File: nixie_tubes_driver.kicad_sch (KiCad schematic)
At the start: 17 parts, among them IC1 TPS61041DBVR, U1 CD40109BPW, U5 CD40109BPW, U6 HV5122PG-G, U7 HV5122PG-G

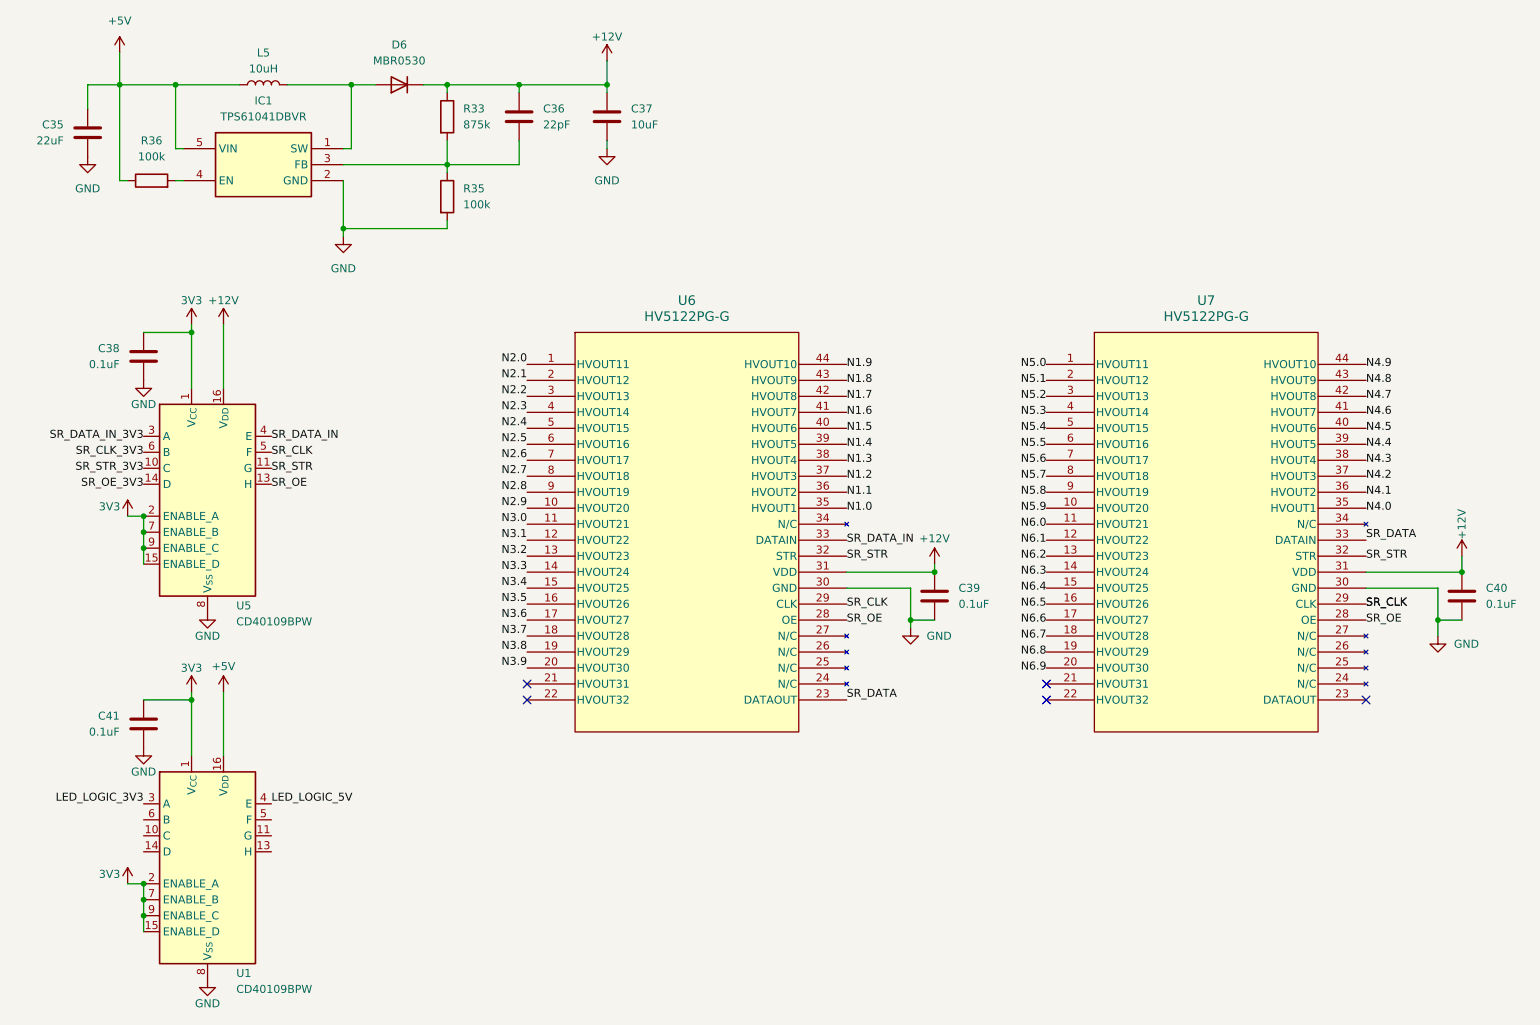
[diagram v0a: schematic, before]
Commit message: Add global labels for nets spanning several sheets
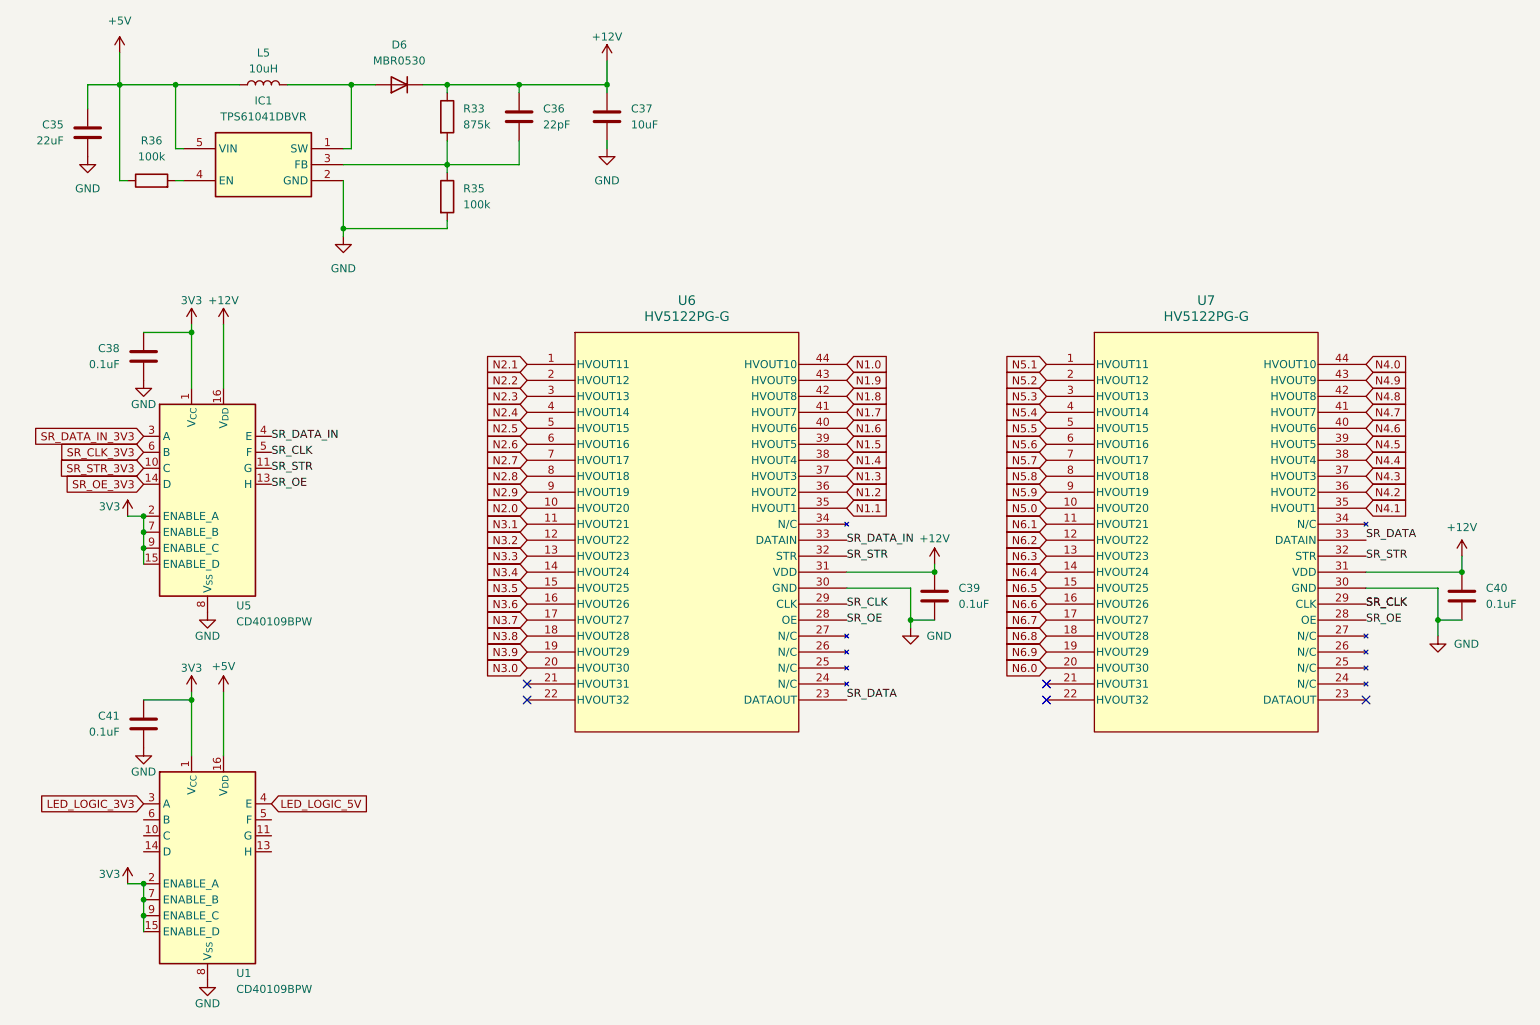
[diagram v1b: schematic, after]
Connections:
- net N1.0: now also U6.44 (HVOUT10); no longer U6.35 (HVOUT1)
- net N1.1: now also U6.35 (HVOUT1); no longer U6.36 (HVOUT2)
- net N1.2: now also U6.36 (HVOUT2); no longer U6.37 (HVOUT3)
- net N1.3: now also U6.37 (HVOUT3); no longer U6.38 (HVOUT4)
- net N1.4: now also U6.38 (HVOUT4); no longer U6.39 (HVOUT5)
- net N1.5: now also U6.39 (HVOUT5); no longer U6.40 (HVOUT6)
- net N1.6: now also U6.40 (HVOUT6); no longer U6.41 (HVOUT7)
- net N1.7: now also U6.41 (HVOUT7); no longer U6.42 (HVOUT8)
- net N1.8: now also U6.42 (HVOUT8); no longer U6.43 (HVOUT9)
- net N1.9: now also U6.43 (HVOUT9); no longer U6.44 (HVOUT10)
- net N2.0: now also U6.10 (HVOUT20); no longer U6.1 (HVOUT11)
- net N2.1: now also U6.1 (HVOUT11); no longer U6.2 (HVOUT12)
- net N2.2: now also U6.2 (HVOUT12); no longer U6.3 (HVOUT13)
- net N2.3: now also U6.3 (HVOUT13); no longer U6.4 (HVOUT14)
- net N2.4: now also U6.4 (HVOUT14); no longer U6.5 (HVOUT15)
- net N2.5: now also U6.5 (HVOUT15); no longer U6.6 (HVOUT16)
- net N2.6: now also U6.6 (HVOUT16); no longer U6.7 (HVOUT17)
- net N2.7: now also U6.7 (HVOUT17); no longer U6.8 (HVOUT18)
- net N2.8: now also U6.8 (HVOUT18); no longer U6.9 (HVOUT19)
- net N2.9: now also U6.9 (HVOUT19); no longer U6.10 (HVOUT20)
- net N3.0: now also U6.20 (HVOUT30); no longer U6.11 (HVOUT21)
- net N3.1: now also U6.11 (HVOUT21); no longer U6.12 (HVOUT22)
- net N3.2: now also U6.12 (HVOUT22); no longer U6.13 (HVOUT23)
- net N3.3: now also U6.13 (HVOUT23); no longer U6.14 (HVOUT24)
- net N3.4: now also U6.14 (HVOUT24); no longer U6.15 (HVOUT25)
- net N3.5: now also U6.15 (HVOUT25); no longer U6.16 (HVOUT26)
- net N3.6: now also U6.16 (HVOUT26); no longer U6.17 (HVOUT27)
- net N3.7: now also U6.17 (HVOUT27); no longer U6.18 (HVOUT28)
- net N3.8: now also U6.18 (HVOUT28); no longer U6.19 (HVOUT29)
- net N3.9: now also U6.19 (HVOUT29); no longer U6.20 (HVOUT30)
- net N4.0: now also U7.44 (HVOUT10); no longer U7.35 (HVOUT1)
- net N4.1: now also U7.35 (HVOUT1); no longer U7.36 (HVOUT2)
- net N4.2: now also U7.36 (HVOUT2); no longer U7.37 (HVOUT3)
- net N4.3: now also U7.37 (HVOUT3); no longer U7.38 (HVOUT4)
- net N4.4: now also U7.38 (HVOUT4); no longer U7.39 (HVOUT5)
- net N4.5: now also U7.39 (HVOUT5); no longer U7.40 (HVOUT6)
- net N4.6: now also U7.40 (HVOUT6); no longer U7.41 (HVOUT7)
- net N4.7: now also U7.41 (HVOUT7); no longer U7.42 (HVOUT8)
- net N4.8: now also U7.42 (HVOUT8); no longer U7.43 (HVOUT9)
- net N4.9: now also U7.43 (HVOUT9); no longer U7.44 (HVOUT10)
- net N5.0: now also U7.10 (HVOUT20); no longer U7.1 (HVOUT11)
- net N5.1: now also U7.1 (HVOUT11); no longer U7.2 (HVOUT12)
- net N5.2: now also U7.2 (HVOUT12); no longer U7.3 (HVOUT13)
- net N5.3: now also U7.3 (HVOUT13); no longer U7.4 (HVOUT14)
- net N5.4: now also U7.4 (HVOUT14); no longer U7.5 (HVOUT15)
- net N5.5: now also U7.5 (HVOUT15); no longer U7.6 (HVOUT16)
- net N5.6: now also U7.6 (HVOUT16); no longer U7.7 (HVOUT17)
- net N5.7: now also U7.7 (HVOUT17); no longer U7.8 (HVOUT18)
- net N5.8: now also U7.8 (HVOUT18); no longer U7.9 (HVOUT19)
- net N5.9: now also U7.9 (HVOUT19); no longer U7.10 (HVOUT20)
- net N6.0: now also U7.20 (HVOUT30); no longer U7.11 (HVOUT21)
- net N6.1: now also U7.11 (HVOUT21); no longer U7.12 (HVOUT22)
- net N6.2: now also U7.12 (HVOUT22); no longer U7.13 (HVOUT23)
- net N6.3: now also U7.13 (HVOUT23); no longer U7.14 (HVOUT24)
- net N6.4: now also U7.14 (HVOUT24); no longer U7.15 (HVOUT25)
- net N6.5: now also U7.15 (HVOUT25); no longer U7.16 (HVOUT26)
- net N6.6: now also U7.16 (HVOUT26); no longer U7.17 (HVOUT27)
- net N6.7: now also U7.17 (HVOUT27); no longer U7.18 (HVOUT28)
- net N6.8: now also U7.18 (HVOUT28); no longer U7.19 (HVOUT29)
- net N6.9: now also U7.19 (HVOUT29); no longer U7.20 (HVOUT30)

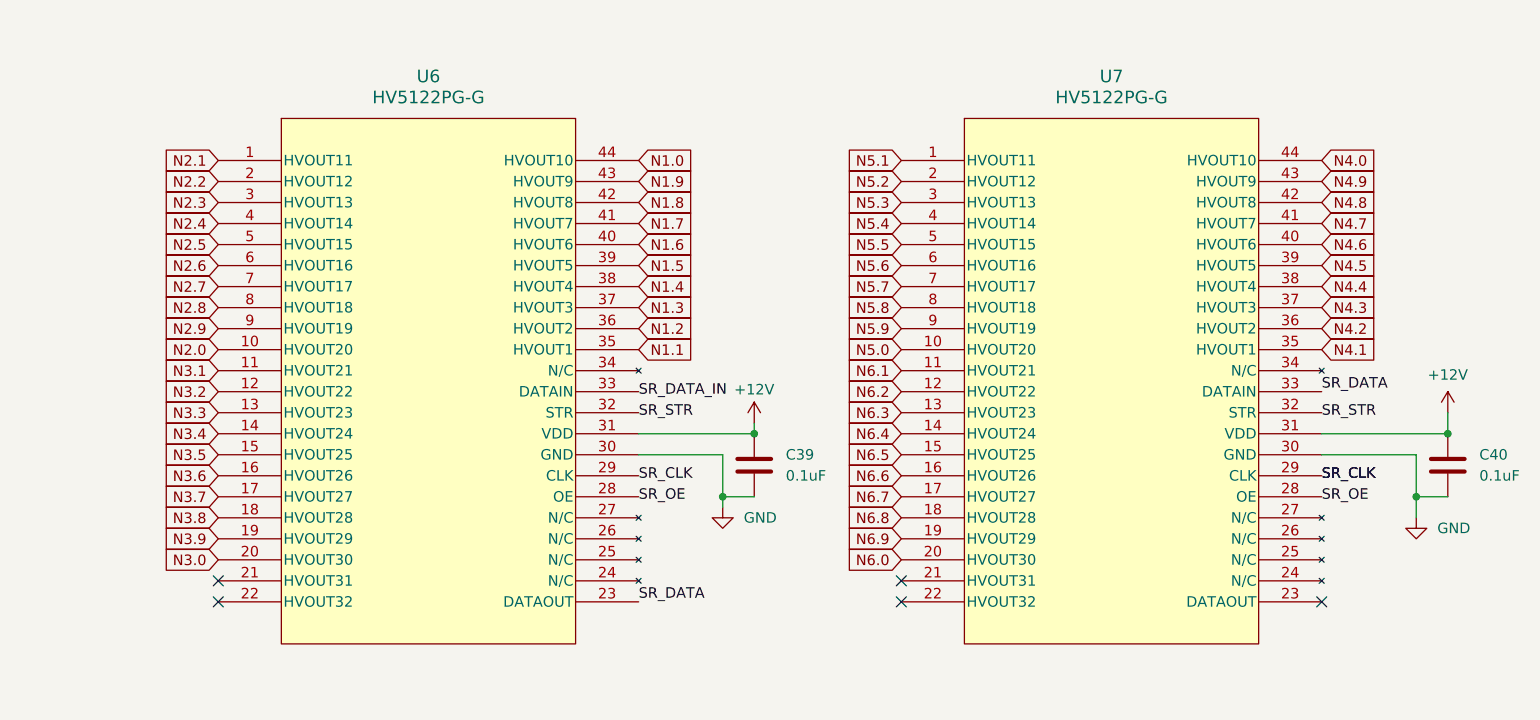
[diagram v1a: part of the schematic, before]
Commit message: Modify nixie tube nets for easier layout
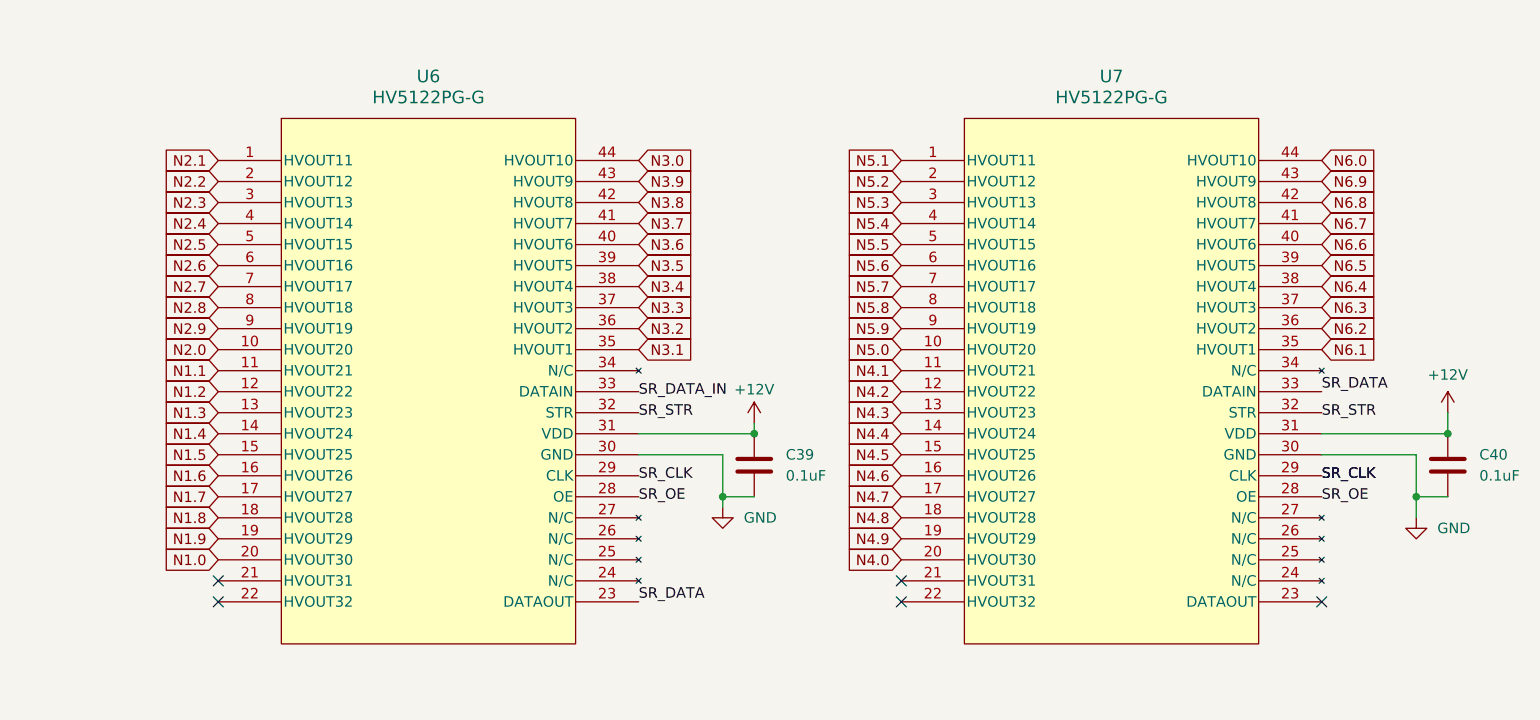
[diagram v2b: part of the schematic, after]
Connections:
- net N1.0: now also U6.20 (HVOUT30); no longer U6.44 (HVOUT10)
- net N1.1: now also U6.11 (HVOUT21); no longer U6.35 (HVOUT1)
- net N1.2: now also U6.12 (HVOUT22); no longer U6.36 (HVOUT2)
- net N1.3: now also U6.13 (HVOUT23); no longer U6.37 (HVOUT3)
- net N1.4: now also U6.14 (HVOUT24); no longer U6.38 (HVOUT4)
- net N1.5: now also U6.15 (HVOUT25); no longer U6.39 (HVOUT5)
- net N1.6: now also U6.16 (HVOUT26); no longer U6.40 (HVOUT6)
- net N1.7: now also U6.17 (HVOUT27); no longer U6.41 (HVOUT7)
- net N1.8: now also U6.18 (HVOUT28); no longer U6.42 (HVOUT8)
- net N1.9: now also U6.19 (HVOUT29); no longer U6.43 (HVOUT9)
- net N3.0: now also U6.44 (HVOUT10); no longer U6.20 (HVOUT30)
- net N3.1: now also U6.35 (HVOUT1); no longer U6.11 (HVOUT21)
- net N3.2: now also U6.36 (HVOUT2); no longer U6.12 (HVOUT22)
- net N3.3: now also U6.37 (HVOUT3); no longer U6.13 (HVOUT23)
- net N3.4: now also U6.38 (HVOUT4); no longer U6.14 (HVOUT24)
- net N3.5: now also U6.39 (HVOUT5); no longer U6.15 (HVOUT25)
- net N3.6: now also U6.40 (HVOUT6); no longer U6.16 (HVOUT26)
- net N3.7: now also U6.41 (HVOUT7); no longer U6.17 (HVOUT27)
- net N3.8: now also U6.42 (HVOUT8); no longer U6.18 (HVOUT28)
- net N3.9: now also U6.43 (HVOUT9); no longer U6.19 (HVOUT29)
- net N4.0: now also U7.20 (HVOUT30); no longer U7.44 (HVOUT10)
- net N4.1: now also U7.11 (HVOUT21); no longer U7.35 (HVOUT1)
- net N4.2: now also U7.12 (HVOUT22); no longer U7.36 (HVOUT2)
- net N4.3: now also U7.13 (HVOUT23); no longer U7.37 (HVOUT3)
- net N4.4: now also U7.14 (HVOUT24); no longer U7.38 (HVOUT4)
- net N4.5: now also U7.15 (HVOUT25); no longer U7.39 (HVOUT5)
- net N4.6: now also U7.16 (HVOUT26); no longer U7.40 (HVOUT6)
- net N4.7: now also U7.17 (HVOUT27); no longer U7.41 (HVOUT7)
- net N4.8: now also U7.18 (HVOUT28); no longer U7.42 (HVOUT8)
- net N4.9: now also U7.19 (HVOUT29); no longer U7.43 (HVOUT9)
- net N6.0: now also U7.44 (HVOUT10); no longer U7.20 (HVOUT30)
- net N6.1: now also U7.35 (HVOUT1); no longer U7.11 (HVOUT21)
- net N6.2: now also U7.36 (HVOUT2); no longer U7.12 (HVOUT22)
- net N6.3: now also U7.37 (HVOUT3); no longer U7.13 (HVOUT23)
- net N6.4: now also U7.38 (HVOUT4); no longer U7.14 (HVOUT24)
- net N6.5: now also U7.39 (HVOUT5); no longer U7.15 (HVOUT25)
- net N6.6: now also U7.40 (HVOUT6); no longer U7.16 (HVOUT26)
- net N6.7: now also U7.41 (HVOUT7); no longer U7.17 (HVOUT27)
- net N6.8: now also U7.42 (HVOUT8); no longer U7.18 (HVOUT28)
- net N6.9: now also U7.43 (HVOUT9); no longer U7.19 (HVOUT29)
